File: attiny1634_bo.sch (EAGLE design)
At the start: 11 parts, among them J1 AVR_SPI_PRG_6NS, Y1 12MHz

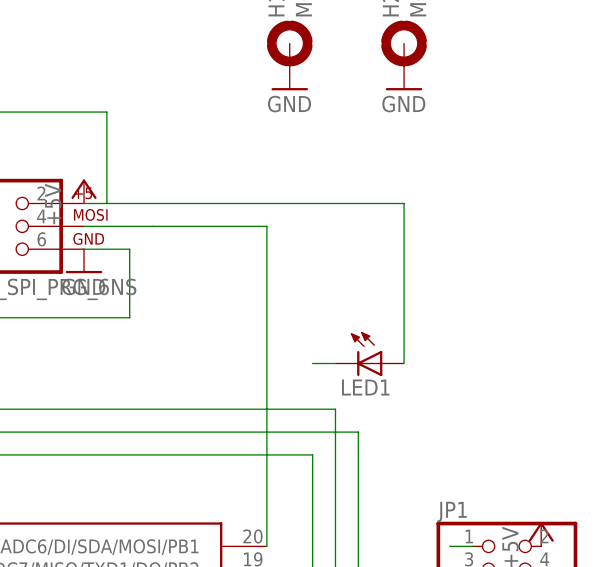
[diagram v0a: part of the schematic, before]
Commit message: add a resistor for the led and move the mcu group right, in preparation for adding a uart header
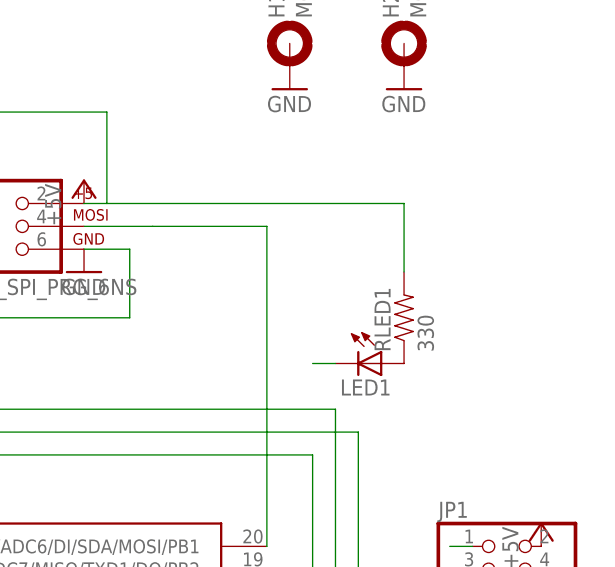
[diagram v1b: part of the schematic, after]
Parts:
- added RLED1: 330, SparkFun-Passives:RESISTOR0603-RES
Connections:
- new net N$1: LED1.A, RLED1.1
- net +5V: now also RLED1.2; no longer LED1.A
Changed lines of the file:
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@@
 <part name="GND1" library="supply1" deviceset="GND" device=""/>
 <part name="U$1" library="attiny1634" deviceset="ATTINY1634" device=""/>
+<part name="RLED1" library="SparkFun-Passives" deviceset="RESISTOR" device="0603-RES" value="330"/>
 </parts>
 <sheets>
@@
 <instance part="GND1" gate="1" x="25.4" y="45.72"/>
 <instance part="U$1" gate="G$1" x="55.88" y="71.12"/>
+<instance part="RLED1" gate="G$1" x="111.76" y="96.52" rot="R90"/>
 </instances>
 <busses>
@@
 <wire x1="78.74" y1="119.38" x2="35.56" y2="119.38" width="0.1524" layer="91"/>
 <wire x1="35.56" y1="119.38" x2="35.56" y2="106.68" width="0.1524" layer="91"/>
-<pinref part="LED1" gate="G$1" pin="A"/>
 <wire x1="78.74" y1="109.22" x2="111.76" y2="109.22" width="0.1524" layer="91"/>
-<wire x1="111.76" y1="109.22" x2="111.76" y2="91.44" width="0.1524" layer="91"/>
+<pinref part="RLED1" gate="G$1" pin="2"/>
+<wire x1="111.76" y1="109.22" x2="111.76" y2="101.6" width="0.1524" layer="91"/>
 </segment>
 <segment>
@@
 </segment>
 </net>
+<net name="N$1" class="0">
+<segment>
+<pinref part="LED1" gate="G$1" pin="A"/>
+<pinref part="RLED1" gate="G$1" pin="1"/>
+</segment>
+</net>

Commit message: space for cable
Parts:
- added FTDI: (no value), pinhead:PINHD-1X6
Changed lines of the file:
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@@
 <part name="U$1" library="attiny1634" deviceset="ATTINY1634" device=""/>
 <part name="RLED1" library="SparkFun-Passives" deviceset="RESISTOR" device="0603-RES" value="330"/>
+<part name="FTDI" library="pinhead" deviceset="PINHD-1X6" device=""/>
 </parts>
 <sheets>
@@
 <instance part="U$1" gate="G$1" x="55.88" y="71.12"/>
 <instance part="RLED1" gate="G$1" x="111.76" y="96.52" rot="R90"/>
+<instance part="FTDI" gate="A" x="-5.08" y="78.74" rot="R180"/>
 </instances>
 <busses>

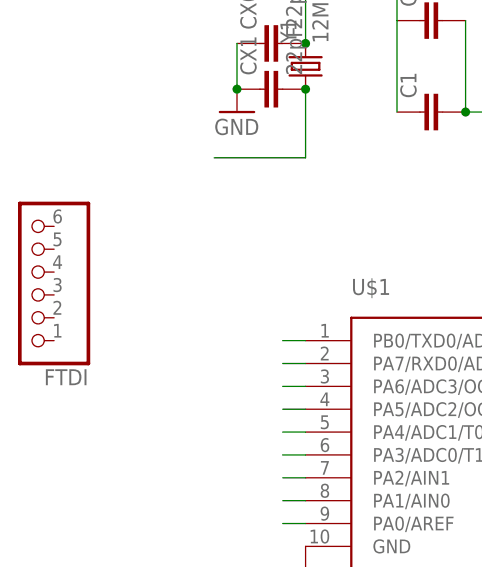
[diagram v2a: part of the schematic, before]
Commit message: added Arduino style FTDI UART header
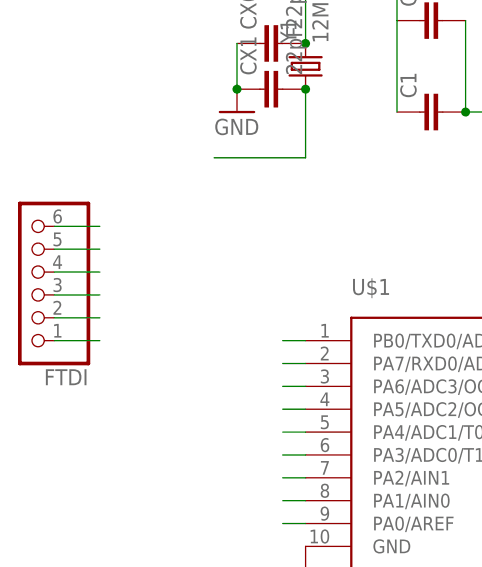
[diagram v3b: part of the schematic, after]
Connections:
- removed net PA7: JP1.19
- new net CTS: FTDI.2
- new net PA7/RX0: FTDI.4, JP1.19
- net +5V: now also FTDI.3
- net GND: now also FTDI.1
- net PB0/TXD0: now also FTDI.5
- net PC3/-RESET: now also FTDI.6
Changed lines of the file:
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@@
 <pinref part="GND1" gate="1" pin="GND"/>
+</segment>
+<segment>
+<pinref part="FTDI" gate="A" pin="1"/>
+<wire x1="-2.54" y1="71.12" x2="2.54" y2="71.12" width="0.1524" layer="91"/>
 </segment>
 </net>
@@
 <pinref part="U$1" gate="G$1" pin="VCC"/>
 </segment>
+<segment>
+<pinref part="FTDI" gate="A" pin="3"/>
+<wire x1="-2.54" y1="76.2" x2="2.54" y2="76.2" width="0.1524" layer="91"/>
+</segment>
 </net>
 <net name="PB1/ADC6/RX1" class="0">
@@
 <pinref part="U$1" gate="G$1" pin="-RESET/PC3"/>
 </segment>
+<segment>
+<pinref part="FTDI" gate="A" pin="6"/>
+<wire x1="-2.54" y1="83.82" x2="2.54" y2="83.82" width="0.1524" layer="91"/>
+</segment>
 </net>
 <net name="PC5/XTAL1" class="0">
@@
 </segment>
 </net>
-<net name="PA7" class="0">
+<net name="PA7/RX0" class="0">
 <segment>
 <pinref part="JP1" gate="A" pin="19"/>
@@
 <wire x1="25.4" y1="68.58" x2="22.86" y2="68.58" width="0.1524" layer="91"/>
 </segment>
+<segment>
+<pinref part="FTDI" gate="A" pin="4"/>
+<wire x1="-2.54" y1="78.74" x2="2.54" y2="78.74" width="0.1524" layer="91"/>
+</segment>
 </net>
 <net name="PA6" class="0">
@@
 <pinref part="U$1" gate="G$1" pin="PB0/TXD0/ADC5"/>
 <wire x1="25.4" y1="71.12" x2="22.86" y2="71.12" width="0.1524" layer="91"/>
+</segment>
+<segment>
+<pinref part="FTDI" gate="A" pin="5"/>
+<wire x1="-2.54" y1="81.28" x2="2.54" y2="81.28" width="0.1524" layer="91"/>
 </segment>
 </net>
@@
 </segment>
 </net>
+<net name="CTS" class="0">
+<segment>
+<pinref part="FTDI" gate="A" pin="2"/>
+<wire x1="-2.54" y1="73.66" x2="2.54" y2="73.66" width="0.1524" layer="91"/>
+</segment>
+</net>

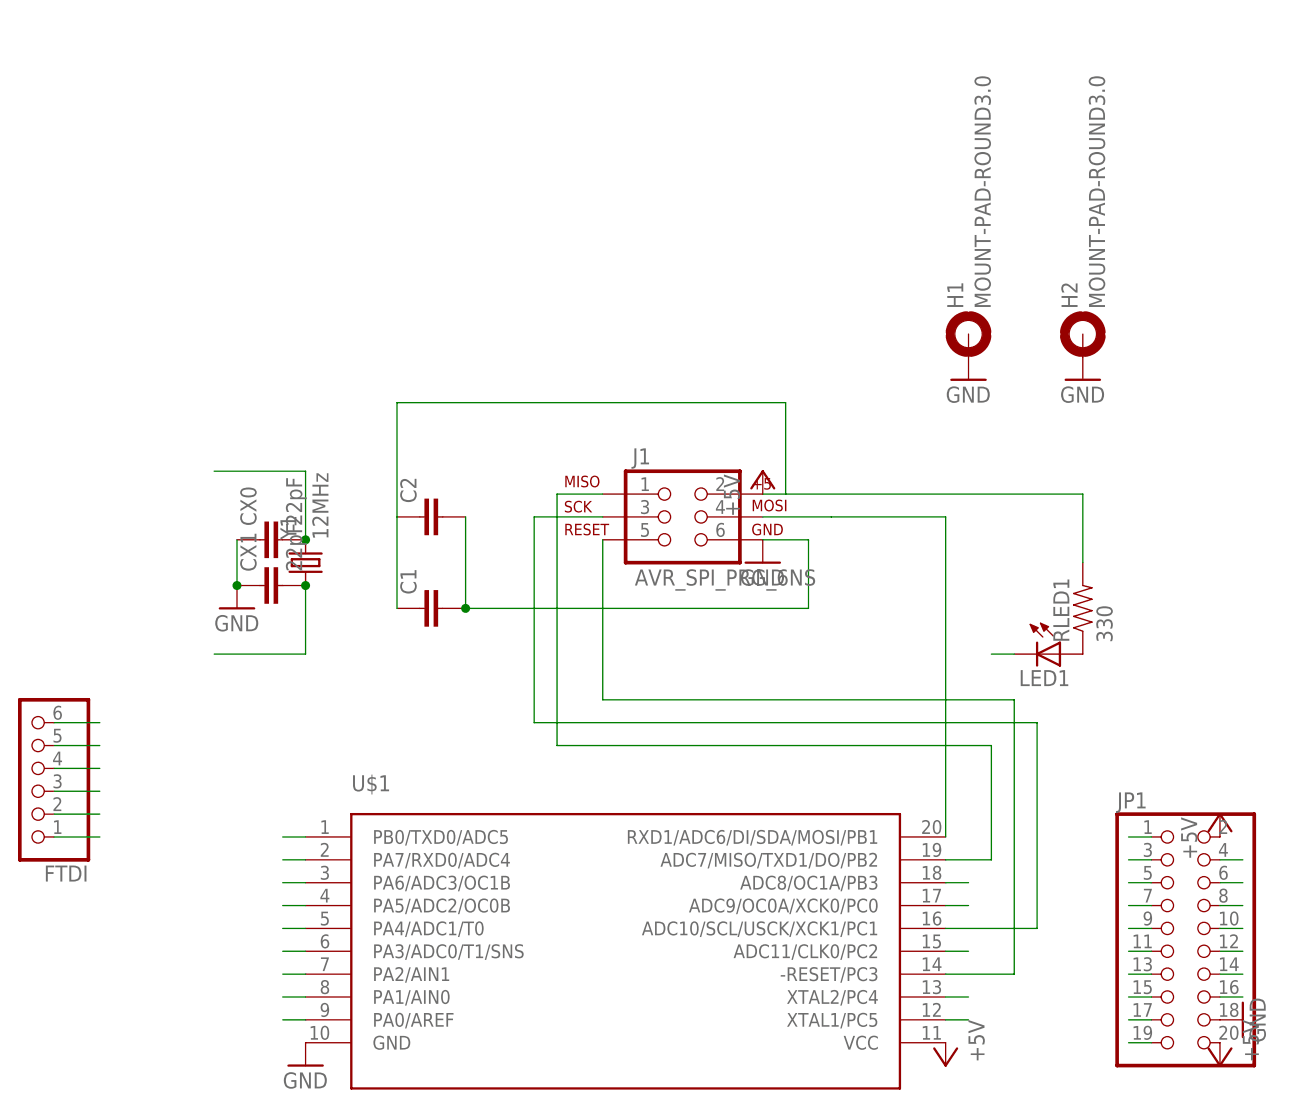
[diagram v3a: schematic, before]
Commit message: args, the PORTA pins did not get reconnected when I fixed the mcu part
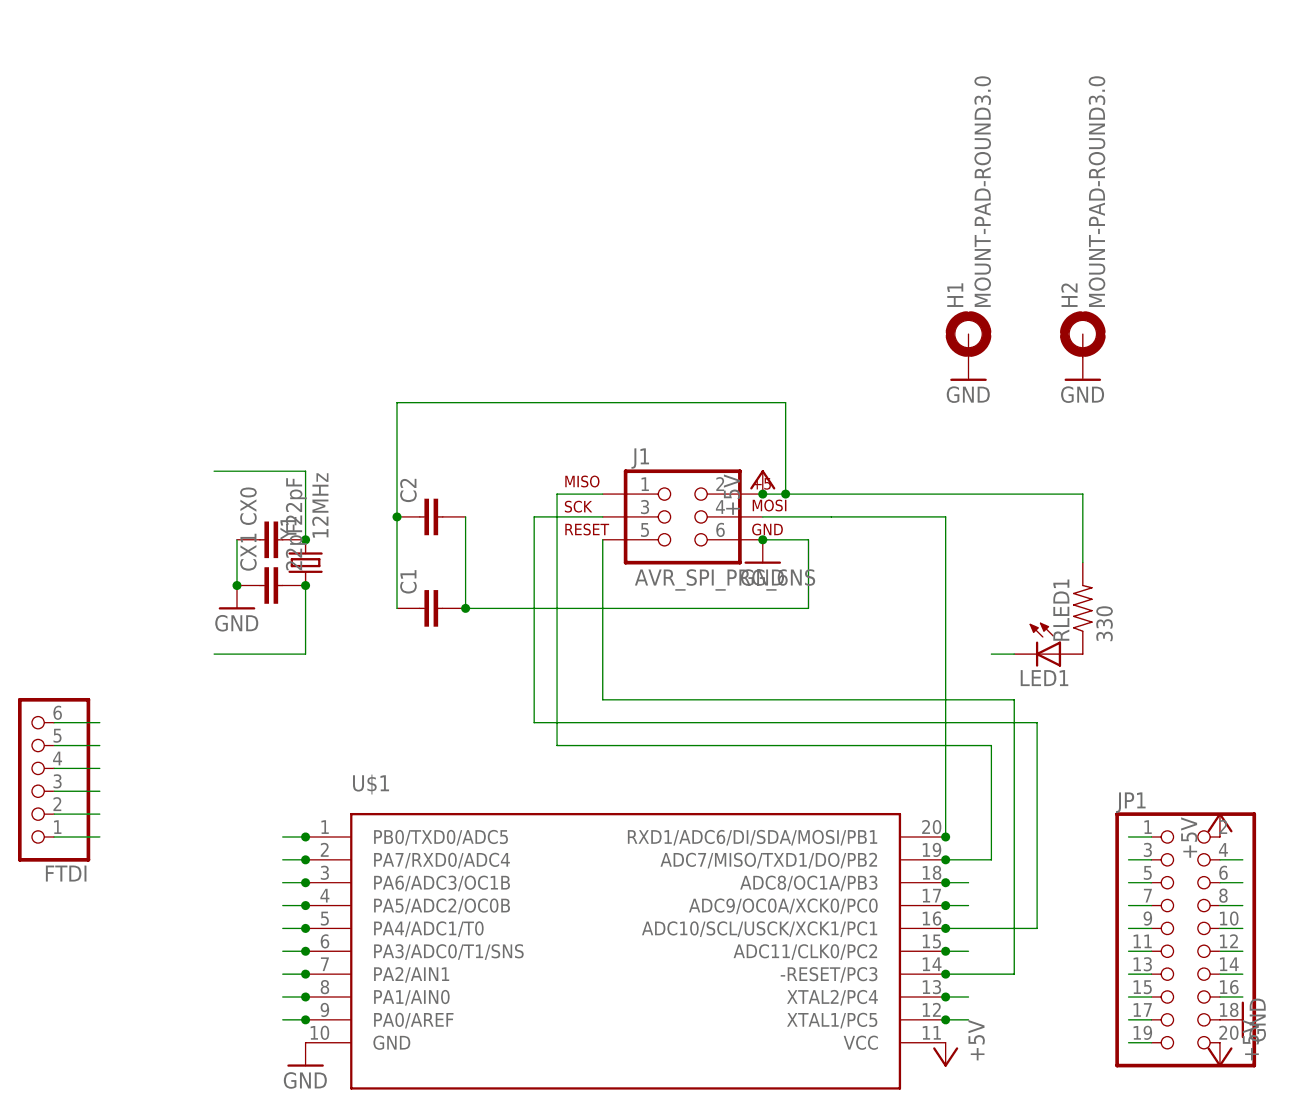
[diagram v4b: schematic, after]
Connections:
- removed net PB1/ADC6/RX1: JP1.14
- net PA0: now also U$1.PA0/AREF
- net PA1: now also U$1.PA1/AIN0
- net PA2: now also U$1.PA2/AIN1
- net PA3: now also U$1.PA3/ADC0/T1/SNS
- net PA4: now also U$1.PA4/ADC1/T0
- net PA5: now also U$1.PA5/ADC2/OC0B
- net PA6: now also U$1.PA6/ADC3/OC1B
- net PA7/RX0: now also U$1.PA7/RXD0/ADC4
- net PB0/TXD0: now also JP1.16
- net PB1/MOSI/ADC6: now also JP1.14; no longer JP1.16
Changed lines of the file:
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@@
 <wire x1="81.28" y1="96.52" x2="81.28" y2="104.14" width="0.1524" layer="91"/>
 <wire x1="81.28" y1="104.14" x2="76.2" y2="104.14" width="0.1524" layer="91"/>
+<junction x="76.2" y="104.14"/>
 </segment>
 <segment>
@@
 <pinref part="RLED1" gate="G$1" pin="2"/>
 <wire x1="111.76" y1="109.22" x2="111.76" y2="101.6" width="0.1524" layer="91"/>
+<junction x="78.74" y="109.22"/>
+<junction x="76.2" y="109.22"/>
+<junction x="35.56" y="106.68"/>
 </segment>
 <segment>
@@
 <pinref part="FTDI" gate="A" pin="3"/>
 <wire x1="-2.54" y1="76.2" x2="2.54" y2="76.2" width="0.1524" layer="91"/>
-</segment>
-</net>
-<net name="PB1/ADC6/RX1" class="0">
-<segment>
-<pinref part="JP1" gate="A" pin="14"/>
-<wire x1="127" y1="55.88" x2="129.54" y2="55.88" width="0.1524" layer="91"/>
 </segment>
 </net>
@@
 <wire x1="50.8" y1="106.68" x2="58.42" y2="106.68" width="0.1524" layer="91"/>
 <pinref part="U$1" gate="G$1" pin="ADC10/SCL/USCK/XCK1/PC1"/>
+<junction x="96.52" y="60.96"/>
 </segment>
 <segment>
@@
 <wire x1="53.34" y1="109.22" x2="58.42" y2="109.22" width="0.1524" layer="91"/>
 <pinref part="U$1" gate="G$1" pin="ADC7/MISO/TXD1/DO/PB2"/>
+<junction x="96.52" y="68.58"/>
 </segment>
 <segment>
@@
 <wire x1="58.42" y1="86.36" x2="58.42" y2="104.14" width="0.1524" layer="91"/>
 <pinref part="U$1" gate="G$1" pin="-RESET/PC3"/>
+<junction x="96.52" y="55.88"/>
 </segment>
 <segment>
@@
 <wire x1="96.52" y1="50.8" x2="99.06" y2="50.8" width="0.1524" layer="91"/>
 <pinref part="U$1" gate="G$1" pin="XTAL1/PC5"/>
+<junction x="96.52" y="50.8"/>
 </segment>
 <segment>
@@
 <wire x1="96.52" y1="53.34" x2="99.06" y2="53.34" width="0.1524" layer="91"/>
 <pinref part="U$1" gate="G$1" pin="XTAL2/PC4"/>
+<junction x="96.52" y="53.34"/>
 </segment>
 <segment>
@@
 <segment>
 <wire x1="25.4" y1="50.8" x2="22.86" y2="50.8" width="0.1524" layer="91"/>
+<pinref part="U$1" gate="G$1" pin="PA0/AREF"/>
+<junction x="25.4" y="50.8"/>
 </segment>
 <segment>
@@
 <segment>
 <wire x1="25.4" y1="53.34" x2="22.86" y2="53.34" width="0.1524" layer="91"/>
+<pinref part="U$1" gate="G$1" pin="PA1/AIN0"/>
+<junction x="25.4" y="53.34"/>
 </segment>
 <segment>
@@
 <segment>
 <wire x1="25.4" y1="63.5" x2="22.86" y2="63.5" width="0.1524" layer="91"/>
+<pinref part="U$1" gate="G$1" pin="PA5/ADC2/OC0B"/>
+<junction x="25.4" y="63.5"/>
 </segment>
 </net>
@@
 <segment>
 <wire x1="25.4" y1="60.96" x2="22.86" y2="60.96" width="0.1524" layer="91"/>
+<pinref part="U$1" gate="G$1" pin="PA4/ADC1/T0"/>
+<junction x="25.4" y="60.96"/>
 </segment>
 </net>
@@
 <segment>
 <wire x1="25.4" y1="58.42" x2="22.86" y2="58.42" width="0.1524" layer="91"/>
+<pinref part="U$1" gate="G$1" pin="PA3/ADC0/T1/SNS"/>
+<junction x="25.4" y="58.42"/>
 </segment>
 </net>
@@
 <segment>
 <wire x1="25.4" y1="55.88" x2="22.86" y2="55.88" width="0.1524" layer="91"/>
+<pinref part="U$1" gate="G$1" pin="PA2/AIN1"/>
+<junction x="25.4" y="55.88"/>
 </segment>
 </net>
@@
 <segment>
 <wire x1="25.4" y1="68.58" x2="22.86" y2="68.58" width="0.1524" layer="91"/>
+<pinref part="U$1" gate="G$1" pin="PA7/RXD0/ADC4"/>
+<junction x="25.4" y="68.58"/>
 </segment>
 <segment>
@@
 <segment>
 <wire x1="25.4" y1="66.04" x2="22.86" y2="66.04" width="0.1524" layer="91"/>
+<pinref part="U$1" gate="G$1" pin="PA6/ADC3/OC1B"/>
+<junction x="25.4" y="66.04"/>
 </segment>
 </net>
@@
 <wire x1="96.52" y1="66.04" x2="99.06" y2="66.04" width="0.1524" layer="91"/>
 <pinref part="U$1" gate="G$1" pin="ADC8/OC1A/PB3"/>
+<junction x="96.52" y="66.04"/>
 </segment>
 <segment>
@@
 <wire x1="96.52" y1="63.5" x2="99.06" y2="63.5" width="0.1524" layer="91"/>
 <pinref part="U$1" gate="G$1" pin="ADC9/OC0A/XCK0/PC0"/>
+<junction x="96.52" y="63.5"/>
 </segment>
 <segment>
@@
 <wire x1="96.52" y1="58.42" x2="99.06" y2="58.42" width="0.1524" layer="91"/>
 <pinref part="U$1" gate="G$1" pin="ADC11/CLK0/PC2"/>
+<junction x="96.52" y="58.42"/>
 </segment>
 <segment>
@@
 <pinref part="U$1" gate="G$1" pin="PB0/TXD0/ADC5"/>
 <wire x1="25.4" y1="71.12" x2="22.86" y2="71.12" width="0.1524" layer="91"/>
+<junction x="25.4" y="71.12"/>
 </segment>
 <segment>
 <pinref part="FTDI" gate="A" pin="5"/>
 <wire x1="-2.54" y1="81.28" x2="2.54" y2="81.28" width="0.1524" layer="91"/>
+</segment>
+<segment>
+<pinref part="JP1" gate="A" pin="16"/>
+<wire x1="127" y1="53.34" x2="129.54" y2="53.34" width="0.1524" layer="91"/>
 </segment>
 </net>
@@
 <wire x1="96.52" y1="71.12" x2="96.52" y2="106.68" width="0.1524" layer="91"/>
 <wire x1="96.52" y1="106.68" x2="83.82" y2="106.68" width="0.1524" layer="91"/>
-</segment>
-<segment>
-<pinref part="JP1" gate="A" pin="16"/>
-<wire x1="127" y1="53.34" x2="129.54" y2="53.34" width="0.1524" layer="91"/>
-</segment>
-</net>
+<junction x="96.52" y="71.12"/>
+</segment>
+<segment>
+<pinref part="JP1" gate="A" pin="14"/>
+<wire x1="127" y1="55.88" x2="129.54" y2="55.88" width="0.1524" layer="91"/>
+</segment>
+</net>

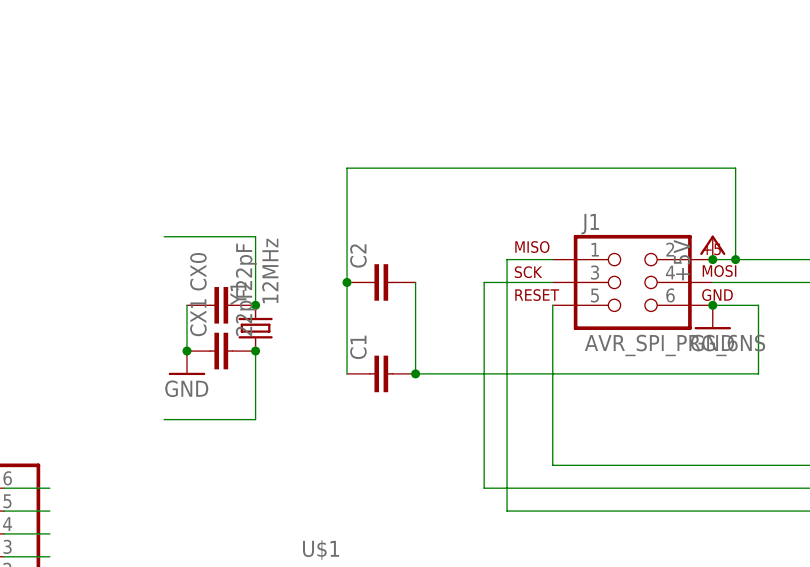
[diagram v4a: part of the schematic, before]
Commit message: Eagle autorouted
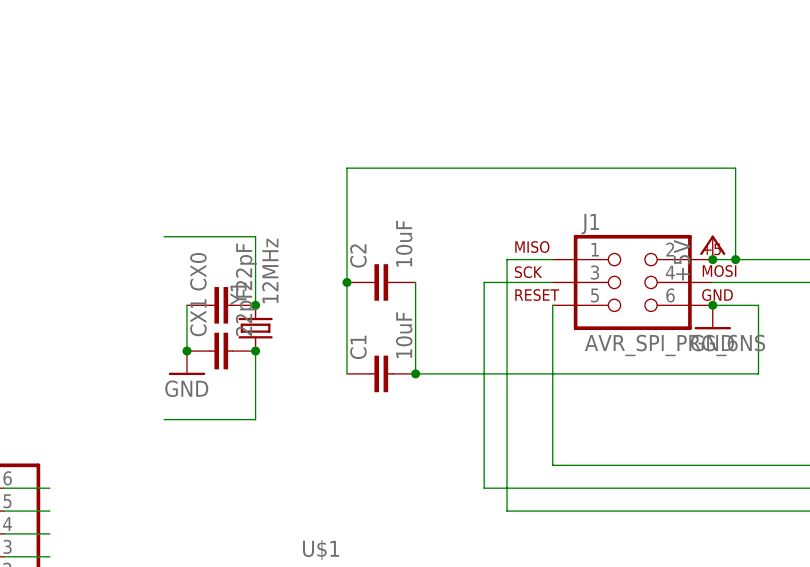
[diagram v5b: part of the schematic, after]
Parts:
- C1, C2: value (none) -> 10uF
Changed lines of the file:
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@@
 <part name="GND5" library="supply1" deviceset="GND" device=""/>
 <part name="P+5" library="supply1" deviceset="+5V" device=""/>
-<part name="C1" library="rcl" deviceset="C-EU" device="C0805"/>
+<part name="C1" library="rcl" deviceset="C-EU" device="C0805" value="10uF"/>
 <part name="LED1" library="SparkFun-LED" deviceset="LED" device="0603"/>
-<part name="C2" library="rcl" deviceset="C-EU" device="C0805"/>
+<part name="C2" library="rcl" deviceset="C-EU" device="C0805" value="10uF"/>
 <part name="CX0" library="rcl" deviceset="C-EU" device="C0603" value="22pF"/>
 <part name="CX1" library="rcl" deviceset="C-EU" device="C0603" value="22pF"/>
